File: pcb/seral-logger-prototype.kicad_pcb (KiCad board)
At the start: 2 copper layers, 108 x 23 mm, 49 parts, among them J1 Conn_ARM_JTAG_SWD_10, J2 Conn_01x04_Female, J3 Conn_01x04_Female, SW1 Rotary_Encoder_Switch_RGB, SW2 SW_SPST, U1 STM32G070KBT6, U2 74LVC3G17, U3 TLV70228_SOT23-5, U4 sn74lv1t34, U5 TLV61046ADB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

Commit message: Layout seems plausible: start routing
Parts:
- removed C5: 100nF, Capacitor_SMD:C_0402_1005Metric
- removed R3, R4: 220, Resistor_SMD:R_0402_1005Metric
- added H2: MountingHole_Pad, MountingHole:MountingHole_2.2mm_M2_Pad_Via, F.Cu at (26.5, 57.5)
- added H3: MountingHole_Pad, MountingHole:MountingHole_2.2mm_M2_Pad_Via, F.Cu at (115.3, 81.7)
- added R1: 220, Resistor_SMD:R_0402_1005Metric, F.Cu at (31.0, 79.0)
- BT1: footprint Jitter_Footprints:BatteryHolder_Keystone_1042(P)__1043(P)_1x18650 -> Jitter_Footprints:BatteryHolder_Keystone_1043(p)_1x18650
- R13, R5, R7: footprint Resistor_SMD:R_0402_1005Metric -> Resistor_SMD:R_0603_1608Metric
- SW1: value Rotary_Encoder_Switch_RGB -> Rotary_Encoder_Switch_DualLED; footprint Jitter_Footprints:Encoder_Switch_RGB_EC12PLRGBSDVBF -> Jitter_Footprints:PEL12D-4xxxS-Sxxxx; moved to F.Cu
- SW2: value SW_SPST -> SW_SPDT; footprint Button_Switch_SMD:SW_SPDT_CK-JS102011SAQN -> Jitter_Footprints:slide_switch_09.03201.02
- moved SW2 73.5 mm to (34.5, 57.3), turned to 0 degrees
- moved L1 67.1 mm to (43.5, 63.0), turned to 270 degrees
- moved C17 66.4 mm to (42.2, 58.2), turned to 270 degrees
- moved U5 59.0 mm to (47.5, 64.4), turned to 90 degrees
- moved U3 55.5 mm to (45.5, 58.0), turned to 0 degrees
- moved R14 55.5 mm to (48.0, 66.8), turned to 180 degrees
- moved C18 54.6 mm to (50.2, 64.4), turned to 90 degrees
- moved C11 54.6 mm to (47.5, 61.0), turned to 180 degrees
- moved R11 53.5 mm to (50.0, 66.8)
- moved TP3 52.8 mm to (44.4, 55.3), turned to 180 degrees
- moved C12 51.7 mm to (48.5, 58.0)
- moved TP4 50.6 mm to (53.0, 65.1), turned to 90 degrees
- moved J2 49.0 mm to (120.0, 65.0), turned to 0 degrees
- moved C3 42.0 mm to (79.5, 68.0)
- moved C6 42.0 mm to (79.5, 66.5)
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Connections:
- R12 pad 1: /SW -> /A
- R13 pad 1: GND -> /A
- R13 pad 2: /SW -> +3V3
- R5 pad 1: /A -> /B
- R6 pad 1: /A -> /B
- R7 pad 1: /B -> /SW
- R8 pad 1: /B -> /SW
- SW1 pad 1: Net-(R2-Pad2) -> GND
- SW1 pad 3: /SW -> Net-(R2-Pad2)
- SW1 pad 4: Net-(R4-Pad2) -> /SW
- U1 pad 21: /encoder_LED_B -> (no net)
- U2 pad 2: /encoder_B -> /encoder_BTN
- U2 pad 5: /encoder_BTN -> /encoder_A
- U2 pad 7: /encoder_A -> /encoder_B
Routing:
- net /A: track 0.00 -> 34.2 mm
- net /SW: track 0.00 -> 25.0 mm
- net /B: track 0.00 -> 24.8 mm
- net GND: track 0.00 -> 20.1 mm, vias 0 -> 13
- net +16V: track 0.00 -> 8.24 mm
- net +3V3: track 0.00 -> 6.61 mm
- net +BATT: track 0.00 -> 5.47 mm
- net Net-(C15-Pad1): track 0.00 -> 2.48 mm
- net Net-(C19-Pad1): track 0.00 -> 2.44 mm
- net Net-(C10-Pad1): track 0.00 -> 2.38 mm
- net Net-(R11-Pad2): track 0.00 -> 2.34 mm
- net /~NRST: track 0.00 -> 1.64 mm
- added copper zone on F.Cu, net +BATT
- added copper zone on F.Cu, net Net-(L1-Pad2)
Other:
- board size 108 x 23 mm -> 100 x 30 mm

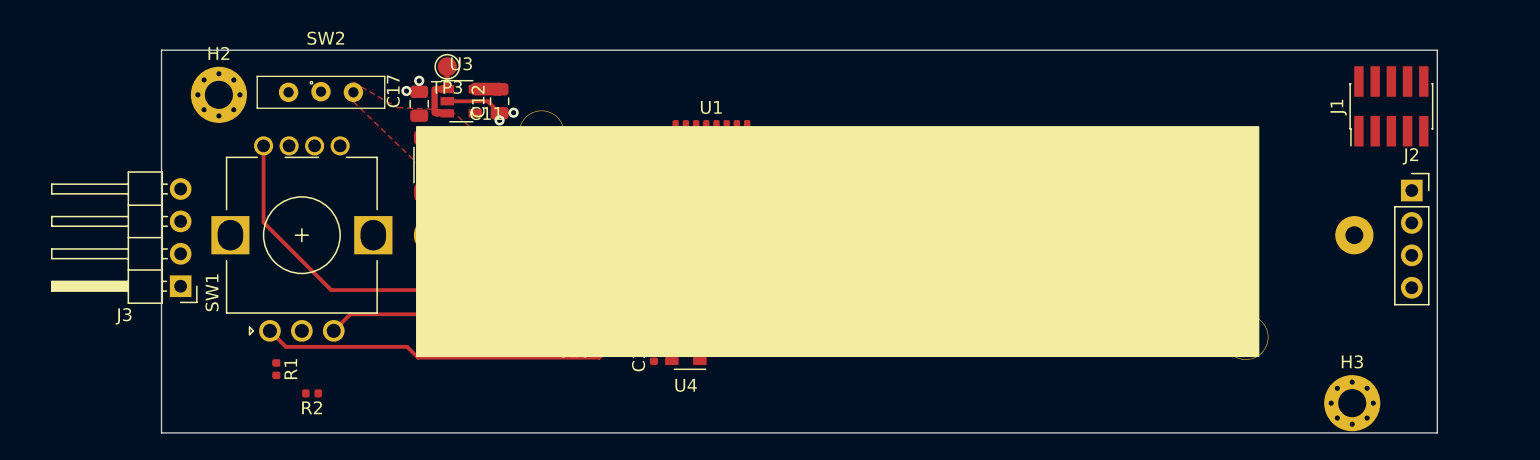
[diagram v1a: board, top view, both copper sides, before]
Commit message: Finish routing and pin swapping
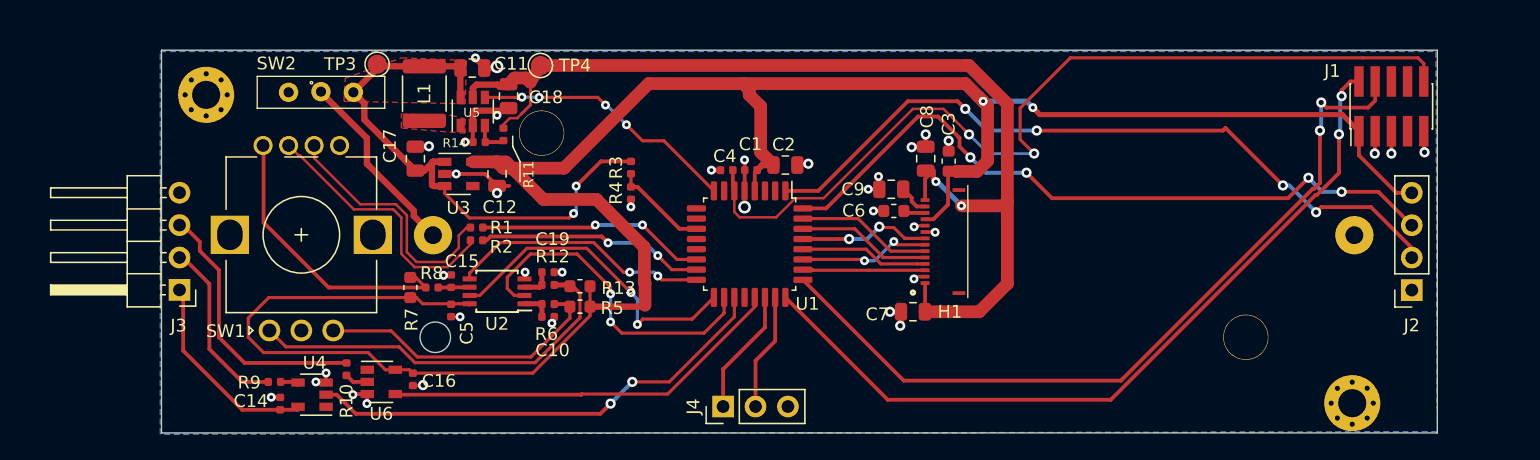
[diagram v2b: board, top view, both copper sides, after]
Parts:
- removed TP1, TP2: TestPoint, TestPoint:TestPoint_Pad_D1.5mm
- added C5: 10nF, Capacitor_SMD:C_0402_1005Metric, F.Cu at (44.7, 74.4)
- added J4: Conn_01x03_Male, Connector_PinHeader_2.54mm:PinHeader_1x03_P2.54mm_Vertical, F.Cu at (66.0, 81.9)
- added R3: 47, Resistor_SMD:R_0402_1005Metric, F.Cu at (58.8, 63.2)
- added R4: 47, Resistor_SMD:R_0402_1005Metric, F.Cu at (58.8, 65.2)
- moved C14 29.5 mm to (31.3, 81.7)
- moved R9 29.5 mm to (30.9, 80.0), turned to 180 degrees
- moved U4 29.5 mm to (33.8, 81.0)
- moved C16 24.9 mm to (41.7, 79.8)
- moved U6 24.8 mm to (39.2, 80.0)
- moved R10 24.3 mm to (36.5, 79.0), turned to 270 degrees
- moved R1 19.2 mm to (46.7, 67.9), turned to 180 degrees
- moved R2 17.6 mm to (46.7, 68.9)
- moved C2 13.0 mm to (70.9, 63.0), turned to 0 degrees
- moved TP4 9.98 mm to (51.7, 55.2)
- moved C1 9.42 mm to (68.2, 63.4)
- moved C4 7.82 mm to (66.3, 63.4)
- moved J2 7.80 mm to (120.0, 72.8), turned to 180 degrees
- moved C18 6.91 mm to (49.2, 57.6)
- moved C3 6.76 mm to (83.7, 62.7), turned to 90 degrees
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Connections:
- J2 pad 2: /RX2 -> /DEBUG_RX3
- J2 pad 3: /TX2 -> /DEBUG_TX3
- U1 pad 1: /encoder_BTN -> /DEBUG_RX3
- U1 pad 10: /RX2 -> (no net)
- U1 pad 11: (no net) -> /BAT_VOLT
- U1 pad 12: /SPI1_SCLK -> (no net)
- U1 pad 14: /SPI1_MOSI -> /encoder_LED_G
- U1 pad 15: (no net) -> /encoder_LED_R
- U1 pad 17: /16V_enable -> /encoder_B
- U1 pad 18: /encoder_LED_R -> /encoder_BTN
- U1 pad 19: /encoder_LED_G -> /TX1
- U1 pad 21: (no net) -> /RX1
- U1 pad 22: (no net) -> /PA11
- U1 pad 23: (no net) -> /PA12
- U1 pad 26: (no net) -> /FRAME_SYNC
- U1 pad 27: /encoder_B -> /SPI1_SCLK
- U1 pad 29: /CMD_DATA -> /SPI1_MOSI
- U1 pad 30: /TX1 -> /~OLED_RST
- U1 pad 31: /RX1 -> /CMD_DATA
- U1 pad 32: /~OLED_RST -> /DEBUG_TX3
- U1 pad 7: /FRAME_SYNC -> (no net)
- U1 pad 8: (no net) -> /16V_enable
- U1 pad 9: /TX2 -> (no net)
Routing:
- net +3V3: track 6.61 -> 179.8 mm, vias 0 -> 2
- net +16V: track 8.24 -> 83.7 mm, vias 0 -> 2
- net /~NRST: track 1.64 -> 70.7 mm, vias 0 -> 2
- net /SWCLK: track 0.00 -> 62.7 mm, vias 0 -> 2
- net /SWDIO: track 0.00 -> 62.3 mm, vias 0 -> 2
- net /DEBUG_RX3: track 0.00 -> 58.0 mm, vias 0 -> 4
- net /DEBUG_TX3: track 0.00 -> 56.0 mm, vias 0 -> 4
- net +BATT: track 5.47 -> 45.0 mm, vias 0 -> 2
- net /TX1: track 0.00 -> 37.3 mm, vias 0 -> 2
- net /RX1: track 0.00 -> 31.8 mm
- net /encoder_BTN: track 0.00 -> 26.2 mm, vias 0 -> 2
- net GND: track 20.1 -> 45.7 mm, vias 13 -> 37
- net /encoder_B: track 0.00 -> 25.2 mm, vias 0 -> 2
- net /16V_enable: track 0.00 -> 21.0 mm, vias 0 -> 4
- net Net-(R2-Pad2): track 0.00 -> 20.9 mm
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- added copper zone on B.Cu, net GND

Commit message: Improve some routing
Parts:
- moved C2 3.75 mm to (67.4, 61.6), turned to 180 degrees
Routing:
- net +3V3: track 179.8 -> 179.2 mm, vias 2 -> 3
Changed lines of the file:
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@@
   )
   (setup
-    (last_trace_width 0.3)
+    (last_trace_width 0.5)
     (user_trace_width 0.2)
     (user_trace_width 0.3)
@@
     (tags capacitor)
     (attr smd)
-    (fp_text reference C4 (at 0.15 1.1) (layer F.SilkS)
+    (fp_text reference C4 (at 1.56 1.1) (layer F.SilkS)
       (effects (font (size 1 1) (thickness 0.15)))
     )
@@
   )
   (module Capacitor_SMD:C_0805_2012Metric (layer F.Cu)
-    (at 70.9 63)
+    (at 67.42 61.61 180)
     (descr "Capacitor SMD 0805 (2012 Metric), square (rectangular) end terminal, IPC_7351 nominal, (Body size source: https://docs.google.com/spreadsheets/d/1BsfQQcO9C6DZCsRaXUlFlo91Tg2WpOkGARC1WS5S8t0/edit?usp=sharing), generated with kicad-footprint-generator")
     (tags capacitor)
     (attr smd)
-    (fp_text reference C2 (at -0.13 -1.6) (layer F.SilkS)
+    (fp_text reference C2 (at 0.09 1.7) (layer F.SilkS)
       (effects (font (size 1 1) (thickness 0.15)))
     )
@@
     (fp_line (start -1 -0.6) (end 1 -0.6) (layer F.Fab) (width 0.1))
     (fp_line (start -1 0.6) (end -1 -0.6) (layer F.Fab) (width 0.1))
-    (pad 2 smd roundrect (at 0.9375 0) (size 0.975 1.4) (layers F.Cu F.Paste F.Mask) (roundrect_rratio 0.25)
-      (net 38 GND))
-    (pad 1 smd roundrect (at -0.9375 0) (size 0.975 1.4) (layers F.Cu F.Paste F.Mask) (roundrect_rratio 0.25)
+    (pad 2 smd roundrect (at 0.9375 0 180) (size 0.975 1.4) (layers F.Cu F.Paste F.Mask) (roundrect_rratio 0.25)
+      (net 38 GND))
+    (pad 1 smd roundrect (at -0.9375 0 180) (size 0.975 1.4) (layers F.Cu F.Paste F.Mask) (roundrect_rratio 0.25)
       (net 2 +3V3))
     (model ${KISYS3DMOD}/Capacitor_SMD.3dshapes/C_0805_2012Metric.wrl
@@
     (tags capacitor)
     (attr smd)
-    (fp_text reference C1 (at 0.04 2.03) (layer F.SilkS)
+    (fp_text reference C1 (at -2.57 0) (layer F.SilkS)
       (effects (font (size 1 1) (thickness 0.15)))
     )
@@
   (segment (start 48.785527 63.248027) (end 53.551973 63.248027) (width 1) (layer F.Cu) (net 2))
   (segment (start 48.3 62.7625) (end 48.785527 63.248027) (width 1) (layer F.Cu) (net 2))
-  (segment (start 67.576973 56.614473) (end 68.0625 57.1) (width 1) (layer F.Cu) (net 2))
   (segment (start 60.185527 56.614473) (end 67.576973 56.614473) (width 1) (layer F.Cu) (net 2))
   (segment (start 53.551973 63.248027) (end 60.185527 56.614473) (width 1) (layer F.Cu) (net 2))
@@
   (segment (start 82.5 67.25) (end 83.649999 66.100001) (width 0.3) (layer F.Cu) (net 2))
   (segment (start 81.85 67.25) (end 82.5 67.25) (width 0.3) (layer F.Cu) (net 2))
-  (segment (start 68.0625 57.5) (end 68.9625 58.4) (width 1) (layer F.Cu) (net 2))
-  (segment (start 68.0625 57.1) (end 68.0625 57.5) (width 1) (layer F.Cu) (net 2))
-  (segment (start 69.085 63) (end 68.685 63.4) (width 0.5) (layer F.Cu) (net 2))
-  (segment (start 69.9625 63) (end 69.085 63) (width 0.5) (layer F.Cu) (net 2))
-  (segment (start 68.9625 62) (end 69.9625 63) (width 1) (layer F.Cu) (net 2))
-  (segment (start 68.9625 58.4) (end 68.9625 62) (width 1) (layer F.Cu) (net 2))
   (segment (start 55.5875 74.1) (end 59.8 74.1) (width 0.5) (layer F.Cu) (net 2))
   (segment (start 59.8 74.1) (end 59.9 74) (width 0.5) (layer F.Cu) (net 2))
@@
   (segment (start 48.3 65.2) (end 48.3 64.6375) (width 0.3) (layer F.Cu) (net 38))
   (segment (start 47.3625 63.7) (end 48.3 64.6375) (width 0.3) (layer F.Cu) (net 38))
-  (via (at 67.7 62.6) (size 0.7) (drill 0.3) (layers F.Cu B.Cu) (net 38))
   (via (at 37 81) (size 0.7) (drill 0.3) (layers F.Cu B.Cu) (net 38))
   (segment (start 37.05 80.95) (end 37 81) (width 0.3) (layer F.Cu) (net 38))
@@
   (via (at 67.7 66.3) (size 1) (drill 0.6) (layers F.Cu B.Cu) (net 38))
   (segment (start 67.7 64.925) (end 67.7 66.3) (width 0.3) (layer F.Cu) (net 38))
-  (segment (start 67.715 62.615) (end 67.7 62.6) (width 0.3) (layer F.Cu) (net 38))
-  (segment (start 67.715 63.4) (end 67.715 62.615) (width 0.3) (layer F.Cu) (net 38))
   (via (at 65.1 63.4) (size 0.7) (drill 0.3) (layers F.Cu B.Cu) (net 38))
   (segment (start 65.815 63.4) (end 65.1 63.4) (width 0.4) (layer F.Cu) (net 38))
@@
   (via (at 118.4 62.1) (size 0.8) (drill 0.4) (layers F.Cu B.Cu) (net 38))
   (segment (start 118.4 60.35) (end 118.4 62.1) (width 0.3) (layer F.Cu) (net 38))
-  (via (at 72.7 62.9) (size 0.8) (drill 0.4) (layers F.Cu B.Cu) (net 38))
-  (segment (start 72.6 63) (end 72.7 62.9) (width 0.3) (layer F.Cu) (net 38))
-  (segment (start 71.8375 63) (end 72.6 63) (width 0.3) (layer F.Cu) (net 38))
+  (via (at 69.52 63.33) (size 0.8) (drill 0.4) (layers F.Cu B.Cu) (net 2))
+  (segment (start 69.42 63.43) (end 69.52 63.33) (width 0.3) (layer F.Cu) (net 2))
+  (segment (start 68.6575 63.43) (end 69.42 63.43) (width 0.3) (layer F.Cu) (net 2))
+  (segment (start 68.3575 57.395) (end 68.3575 61.61) (width 1) (layer F.Cu) (net 2))
+  (segment (start 67.576973 56.614473) (end 68.3575 57.395) (width 1) (layer F.Cu) (net 2))
+  (segment (start 68.685 61.9375) (end 68.685 63.4) (width 0.5) (layer F.Cu) (net 2))
+  (segment (start 68.3575 61.61) (end 68.685 61.9375) (width 0.5) (layer F.Cu) (net 2))
   (segment (start 83.7 61.1) (end 83.7 61.9125) (width 0.2) (layer F.Cu) (net 38))
   (via (at 42.5 80.24999) (size 0.8) (drill 0.4) (layers F.Cu B.Cu) (net 38))
@@
   (segment (start 41.9 61.5625) (end 42.9275 61.5625) (width 0.3) (layer F.Cu) (net 38))
   (segment (start 42.9275 61.5625) (end 42.96 61.53) (width 0.3) (layer F.Cu) (net 38))
+  (via (at 65.52 61.6) (size 0.8) (drill 0.4) (layers F.Cu B.Cu) (net 38))
+  (segment (start 65.53 61.61) (end 65.52 61.6) (width 0.3) (layer F.Cu) (net 38))
+  (segment (start 66.4825 61.61) (end 65.53 61.61) (width 0.3) (layer F.Cu) (net 38))
+  (segment (start 66.4825 60.6925) (end 66.27 60.48) (width 0.3) (layer F.Cu) (net 38))
+  (via (at 66.27 60.48) (size 0.8) (drill 0.4) (layers F.Cu B.Cu) (net 38))
+  (segment (start 66.4825 61.61) (end 66.4825 60.6925) (width 0.3) (layer F.Cu) (net 38))
   (segment (start 45.3 68.52) (end 45.92 67.9) (width 0.2) (layer F.Cu) (net 39))
   (segment (start 45.92 67.9) (end 46.215 67.9) (width 0.2) (layer F.Cu) (net 39))

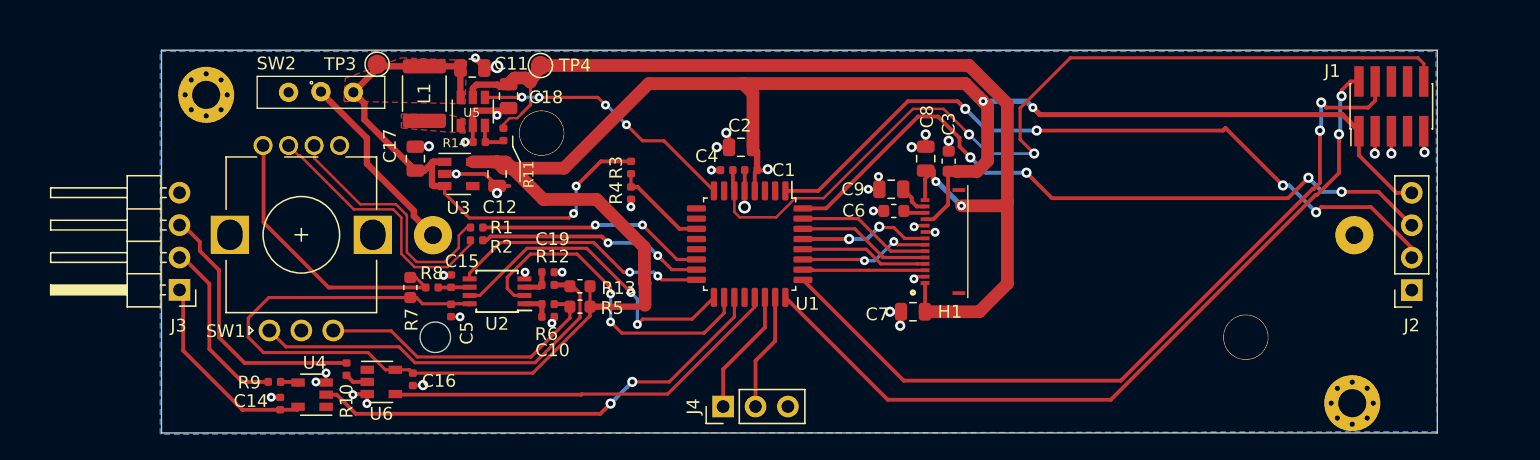
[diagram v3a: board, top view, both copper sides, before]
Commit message: Update slide switch placement and add mounting hole
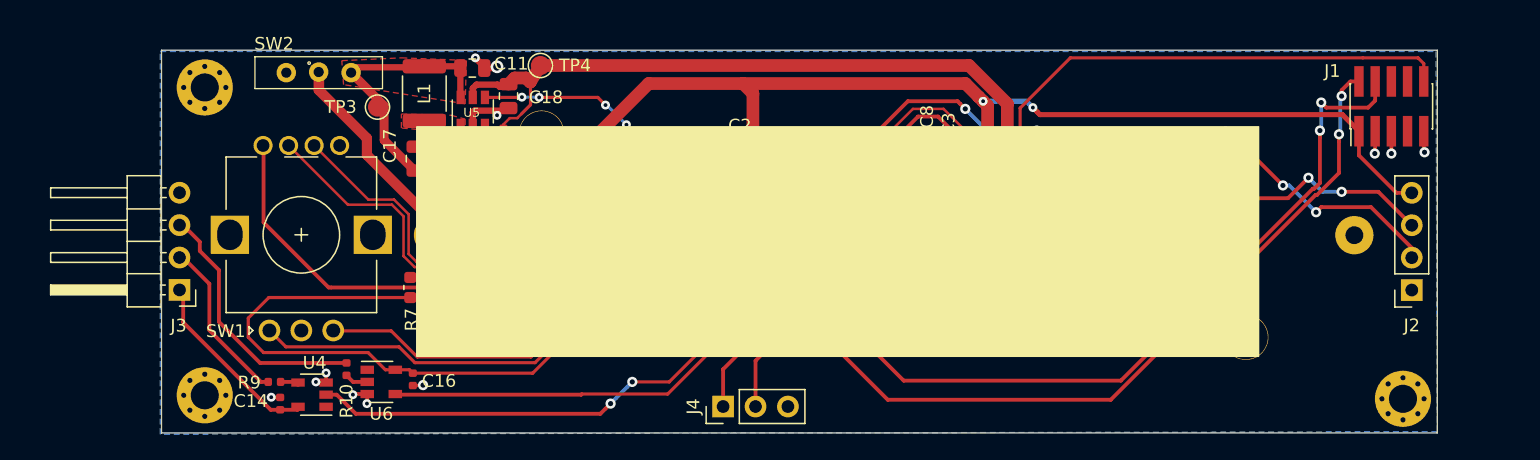
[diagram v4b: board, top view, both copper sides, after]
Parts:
- added H4: MountingHole_Pad, MountingHole:MountingHole_2.2mm_M2_Pad_Via, F.Cu at (25.4, 81.0)
- moved H3 3.99 mm to (119.3, 81.3)
- moved TP3 3.36 mm to (38.9, 58.5)
- moved SW2 1.55 mm to (34.3, 55.8)
- moved H2 0.59 mm to (25.4, 56.9)
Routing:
- net Net-(BT1-Pad1): track 14.9 -> 18.1 mm
- net VBUS: track 15.7 -> 14.4 mm
- net +BATT: track 45.0 -> 46.2 mm
- net /Tx_out: track 13.5 -> 12.6 mm
- net /Rx_in: track 20.8 -> 20.1 mm

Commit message: Uptimize component placement to make room for enclosure
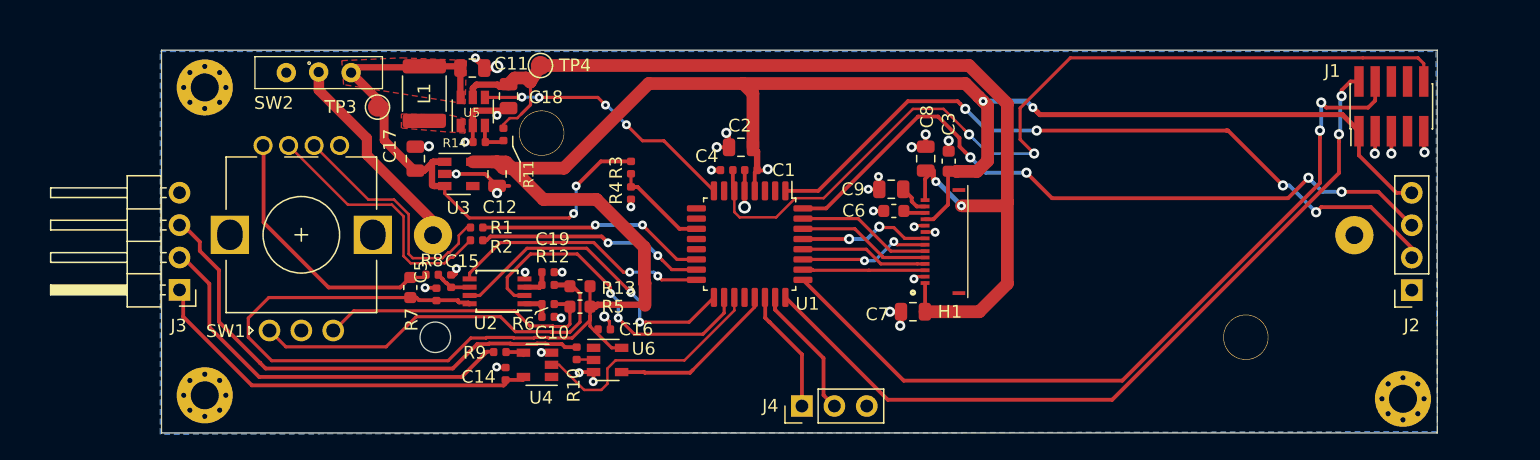
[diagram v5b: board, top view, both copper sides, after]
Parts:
- moved R10 18.1 mm to (54.5, 77.8)
- moved R9 17.8 mm to (48.5, 77.7)
- moved U4 17.8 mm to (51.5, 78.7)
- moved C14 17.8 mm to (49.0, 79.4)
- moved U6 17.8 mm to (57.0, 78.3)
- moved C16 15.5 mm to (56.7, 75.9), turned to 0 degrees
- moved J4 6.18 mm to (72.2, 81.9)
- moved C5 1.71 mm to (43.5, 73.1), turned to 90 degrees
- moved R8 1.00 mm to (43.2, 71.6)
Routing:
- net /Rx_in: track 20.1 -> 39.3 mm
- net /RX1: track 31.8 -> 13.4 mm
- net /Tx_out: track 12.6 -> 30.8 mm
- net /TX1: track 37.3 -> 19.5 mm, vias 2 -> 0
- net VBUS: track 14.4 -> 31.4 mm
- net +3V3: track 179.2 -> 183.0 mm
- net /PA12: track 9.19 -> 10.4 mm
- net /SW: track 22.4 -> 21.3 mm
- net GND: track 46.2 -> 46.3 mm, vias 37 -> 36

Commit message: Add silklayer at bottom side
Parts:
- added G***: LOGO, Logo:GND, B.Cu at (27.9, 65.1)
- added G***: LOGO, Logo:GND, F.Cu at (114.9, 73.0)
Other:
- board text added: "3v"
- board text added: "Rx"
- board text added: "Tx"
- board text added: "Vbus_in Tx Rx"
